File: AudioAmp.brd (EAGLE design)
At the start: 100 x 80 mm, 99 parts, among them X1 22-23-2021, X2 22-23-2021

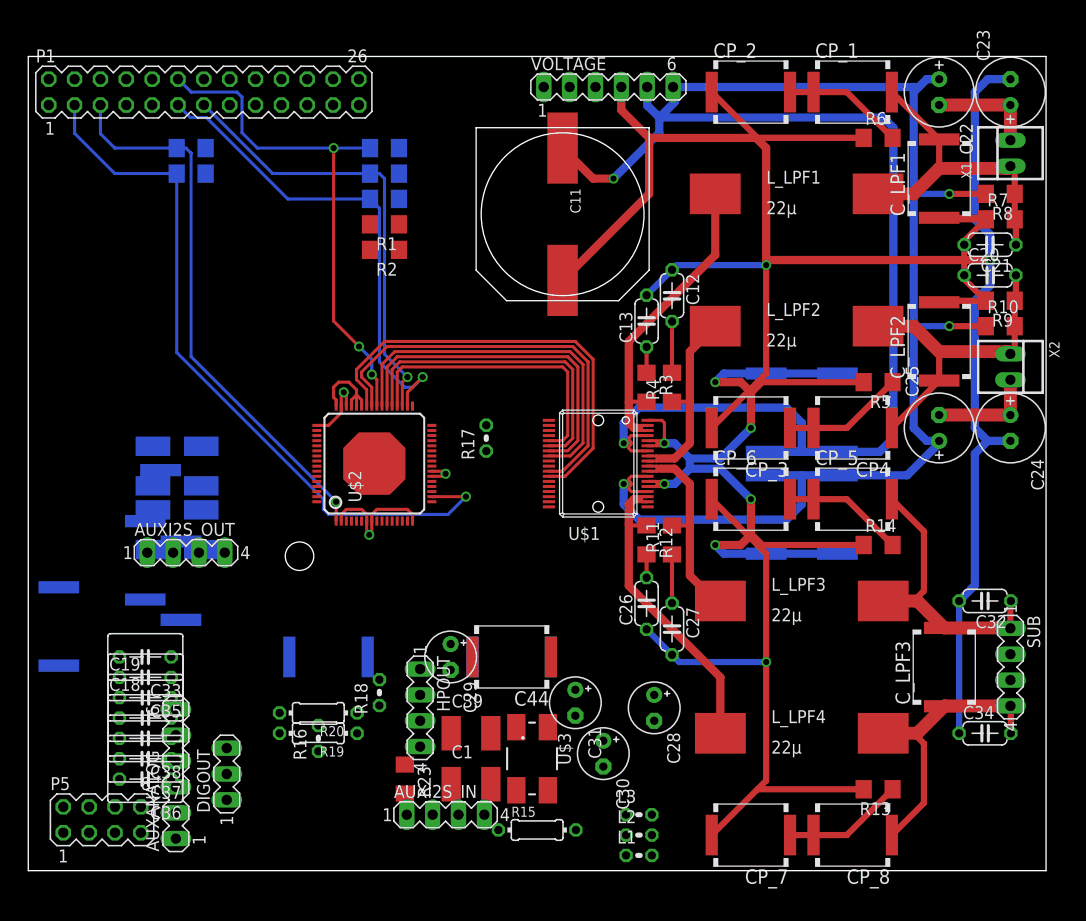
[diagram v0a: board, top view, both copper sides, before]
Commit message: Todo: connect Thermal warning & Amp fault to P1 RPi
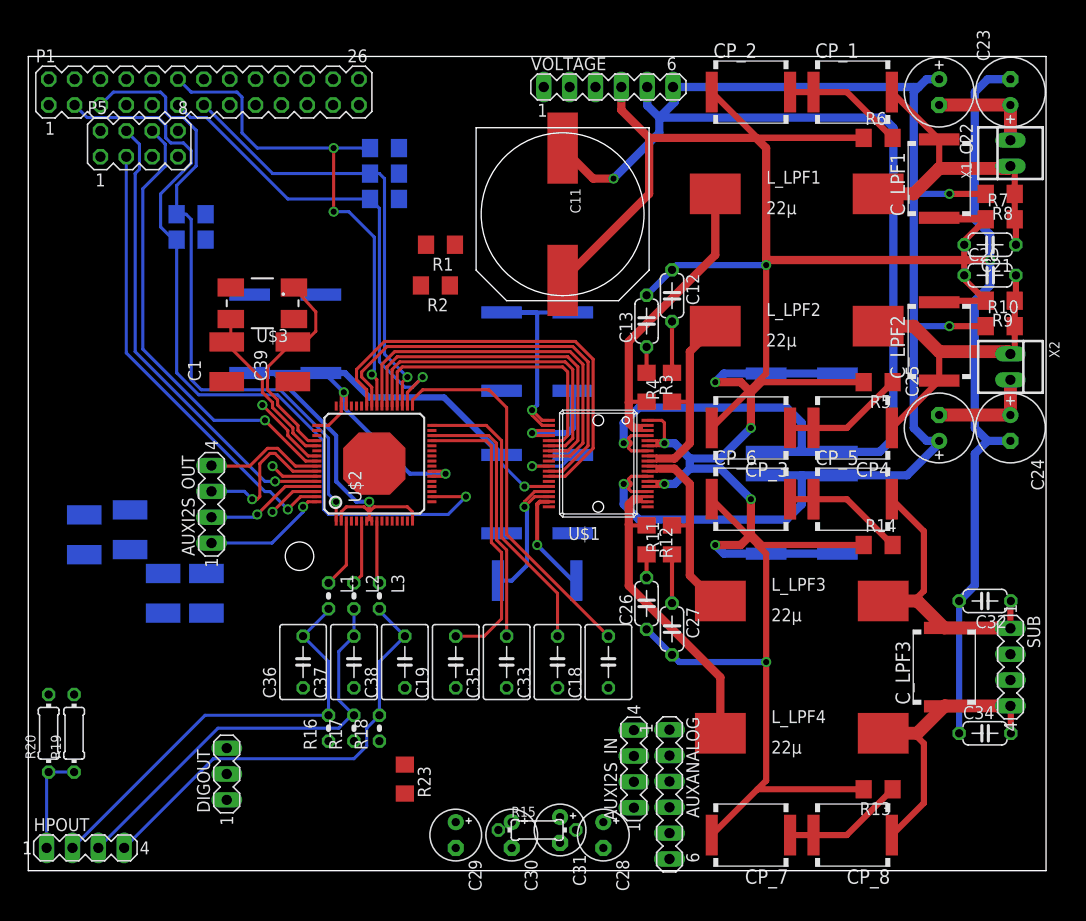
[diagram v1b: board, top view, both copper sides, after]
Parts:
- moved P5 66.5 mm to (10.9, 71.4)
- moved C3 57.3 mm to (53.5, 51.0)
- moved U$3 52.0 mm to (23.0, 55.8), turned to 180 degrees
- moved AUXANALOG 48.5 mm to (63.0, 7.50), turned to 270 degrees
- moved C1 47.9 mm to (19.5, 50.0), turned to 90 degrees
- moved C18 45.8 mm to (57.0, 20.5), turned to 90 degrees
- moved C44 40.9 mm to (21.8, 52.8), flipped to the bottom, turned to 90 degrees
- moved C2 40.6 mm to (46.5, 51.0)
- moved C33 40.5 mm to (52.0, 20.5), turned to 90 degrees
- moved C39 40.5 mm to (26.0, 50.0), turned to 90 degrees
- moved L1 39.8 mm to (29.5, 27.0), turned to 270 degrees
- moved C4 39.4 mm to (53.5, 37.0)
- moved C6 37.7 mm to (50.0, 28.5), turned to 180 degrees
- moved C43 36.9 mm to (28.8, 52.8), turned to 90 degrees
- moved L2 36.6 mm to (32.0, 27.0), turned to 270 degrees
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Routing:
- net VCC3.3: track 22.2 -> 92.4 mm, vias 3 -> 4
- net PCM_FS: track 0.00 -> 45.5 mm, vias 0 -> 1
- net PCM_CLK: track 0.00 -> 44.9 mm, vias 0 -> 1
- net PCM_DOUT: track 0.00 -> 44.5 mm, vias 0 -> 1
- net HPGND: track 0.00 -> 44.0 mm
- net HPLEFT: track 0.00 -> 43.1 mm
- net HPRIGHT: track 0.00 -> 42.2 mm
- net AIN1: track 0.00 -> 37.6 mm
- net AIN3: track 0.00 -> 29.0 mm
- net AIN2: track 0.00 -> 28.7 mm
- net AIN4: track 0.00 -> 26.0 mm
- net VCCSIG: track 0.00 -> 24.9 mm, vias 0 -> 1
- net N$3: track 0.00 -> 21.2 mm
- net N$4: track 0.00 -> 16.9 mm
- net N$6: track 0.00 -> 15.5 mm, vias 0 -> 1
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
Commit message: todo: check analog supply grounding
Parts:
- moved C28 60.6 mm to (7.75, 39.5)
- moved C31 60.1 mm to (3.00, 38.5)
- moved R15 59.1 mm to (9.00, 46.5), turned to 90 degrees
- moved C30 58.8 mm to (4.00, 43.0), turned to 0 degrees
- moved C29 58.2 mm to (4.50, 48.0)
- moved AUXI2S_IN 52.2 mm to (14.0, 35.6)
- moved AUXANALOG 36.7 mm to (26.7, 2.54), turned to 180 degrees
- moved DIGOUT 27.1 mm to (38.1, 29.2), turned to 270 degrees
- moved R23 22.2 mm to (17.9, 20.4)
- moved R16 2.50 mm to (27.0, 14.0)
- moved R18 2.50 mm to (37.0, 14.0)
- moved HPOUT 0.80 mm to (6.35, 2.54)
- moved AUXI2S_OUT 0.49 mm to (17.8, 35.6)
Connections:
- net AMPFAULT: now also P1.16
- net TH-WAR: now also P1.18
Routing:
- net AUX_IN1L: track 0.00 -> 48.0 mm
- net AUX_IN2L: track 0.00 -> 32.7 mm
- net HPLEFT: track 43.1 -> 12.7 mm
- net AUX_IN1R: track 0.00 -> 29.2 mm
- net AUX_IN2R: track 0.00 -> 24.3 mm
- net AUX_PCM_FS: track 4.76 -> 16.6 mm, vias 1 -> 0
- net AUX_PCM_CLK: track 5.18 -> 16.7 mm, vias 1 -> 0
- net N$31: track 0.00 -> 9.42 mm
- net AUX_PCM_DOUT: track 7.71 -> 16.2 mm, vias 1 -> 0
- net N$30: track 0.00 -> 4.32 mm
- net SDA: track 80.2 -> 76.1 mm
- net HPGND: track 44.0 -> 48.0 mm
- net AUX_OUT_D1: track 15.2 -> 12.0 mm, vias 1 -> 0
- net HPRIGHT: track 42.2 -> 44.9 mm
- net AUX_OUT_D2: track 11.8 -> 11.1 mm
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
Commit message: almost done
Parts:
- added SL1: (no value), con-amp-quick:02P
- moved R23 52.4 mm to (35.0, 70.0), flipped to the bottom, turned to 180 degrees
- moved C4 44.2 mm to (22.0, 68.0), flipped to the top
- moved C30 42.7 mm to (44.0, 28.0), turned to 270 degrees
- moved C29 42.5 mm to (38.5, 22.5)
- moved C28 40.0 mm to (44.0, 22.5)
- moved C14 37.6 mm to (47.0, 43.8), turned to 0 degrees
- moved C31 37.0 mm to (38.5, 28.0)
- moved DIGOUT 35.7 mm to (2.54, 26.7)
- moved R15 33.0 mm to (34.2, 25.2)
- moved C15 32.1 mm to (35.8, 43.8), turned to 180 degrees
- moved C16 31.9 mm to (47.0, 39.5), turned to 0 degrees
- moved C17 26.4 mm to (35.8, 39.5), turned to 180 degrees
- moved AUXANALOG 23.2 mm to (49.9, 2.54)
- moved R2 13.5 mm to (35.0, 70.0), turned to 0 degrees
- moved R1 12.1 mm to (35.0, 72.2), turned to 0 degrees
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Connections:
- net AGND: now also SL1.1
- net AVDD: now also SL1.2; no longer VOLTAGE.2
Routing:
- net VCC3.3: track 92.4 -> 201.6 mm, vias 4 -> 5
- net AGND: track 0.00 -> 92.2 mm
- net MUTE: track 0.00 -> 56.5 mm, vias 0 -> 3
- net TH-WAR: track 0.00 -> 56.0 mm, vias 0 -> 2
- net AMPFAULT: track 6.11 -> 60.5 mm, vias 1 -> 2
- net N$17: track 0.00 -> 39.6 mm, vias 0 -> 1
- net N$1: track 0.00 -> 33.3 mm, vias 0 -> 1
- net AVDD: track 0.00 -> 30.2 mm, vias 0 -> 1
- net AUX_IN2L: track 32.7 -> 5.69 mm
- net HPLEFT: track 12.7 -> 35.5 mm
- net AUX_IN1R: track 29.2 -> 8.35 mm
- net AUX_IN1L: track 48.0 -> 27.8 mm
- net N$2: track 0.00 -> 15.2 mm
- net AIN3: track 29.0 -> 43.0 mm
- net AIN4: track 26.0 -> 38.3 mm
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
